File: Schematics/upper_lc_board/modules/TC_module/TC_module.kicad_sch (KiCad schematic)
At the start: 10 parts, among them J7 Screw_Terminal_01x02

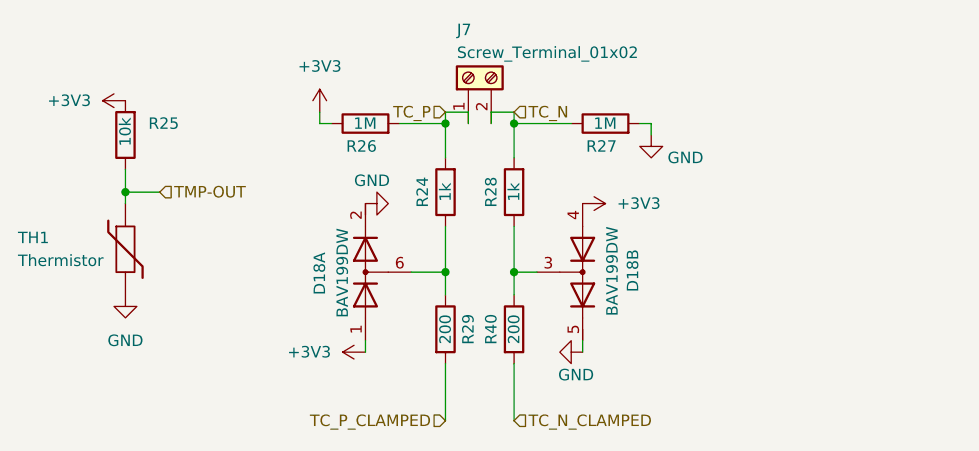
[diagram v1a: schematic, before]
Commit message: add references to caps, ferrite bead footprint, LDO datasheet
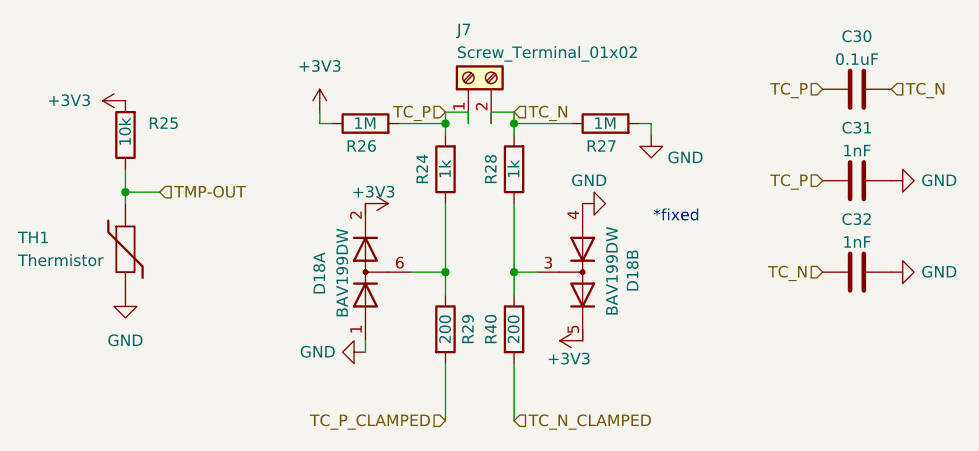
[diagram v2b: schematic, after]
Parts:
- added C30: 0.1uF, Capacitor_SMD:C_0805_2012Metric, symbol Device:C
- added C31, C32: 1nF, Capacitor_SMD:C_0603_1608Metric, symbol Device:C
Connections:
- net +3V3: now also D18.2 (K2), D18.5 (K4); no longer D18.1 (A1), D18.4 (A3)
- net GND: now also D18.1 (A1), D18.4 (A3), C31.1, C32.1; no longer D18.2 (K2), D18.5 (K4)
- net TC_N: now also C30.1, C32.2
- net TC_P: now also C30.2, C31.2
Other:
- note added: "*fixed"
- company: (none) -> Queen's Rocket Engineering Team
- title: (none) -> Thermocouple Circuitry
- moved on the sheet: R24, R28
